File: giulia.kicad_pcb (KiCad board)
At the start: 2 copper layers, 242.2 x 113.8 mm, 138 parts, among them J1 AVR-ISP-6, J2 0548190519, M2,5 MountingHole_2.7mm_M2.5_ISO73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, SW1 RESET, SW2 BOOT, U1 ATmega32A-PU, Y1 16 MHz

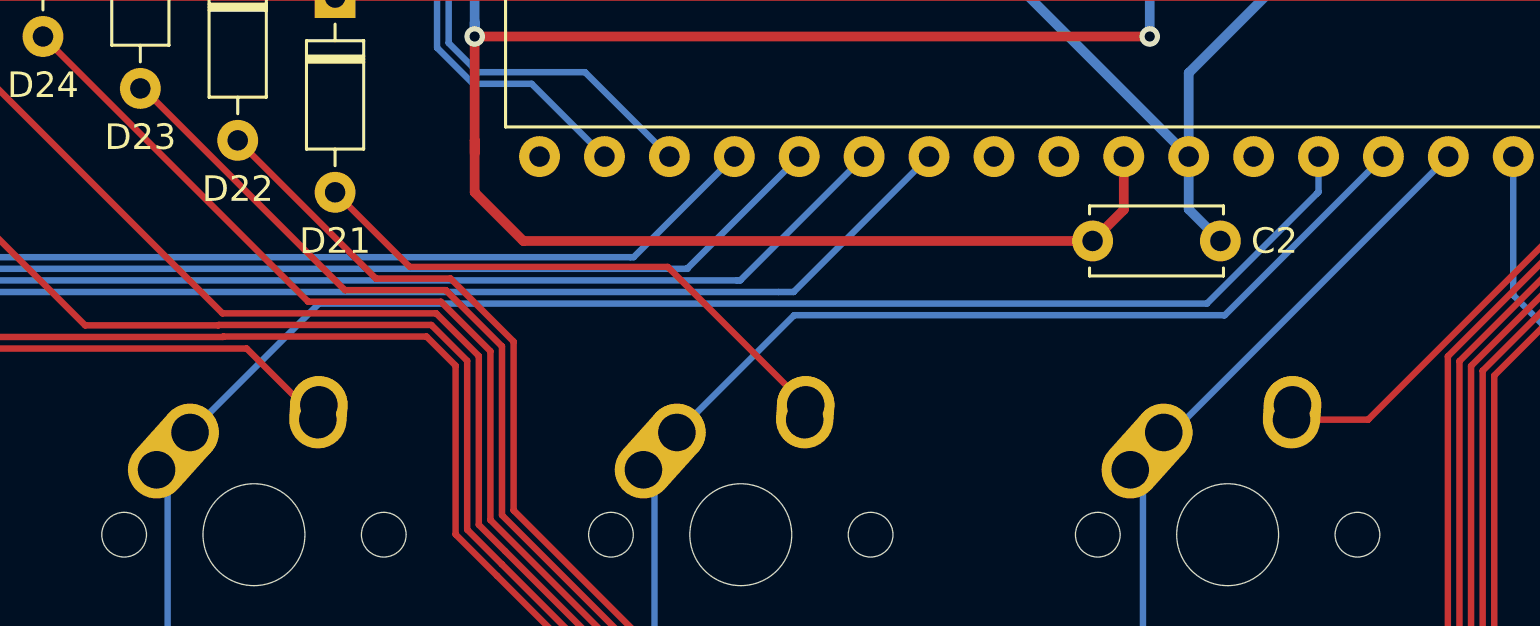
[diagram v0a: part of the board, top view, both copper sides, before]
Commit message: moved cols 4,5 to better pins
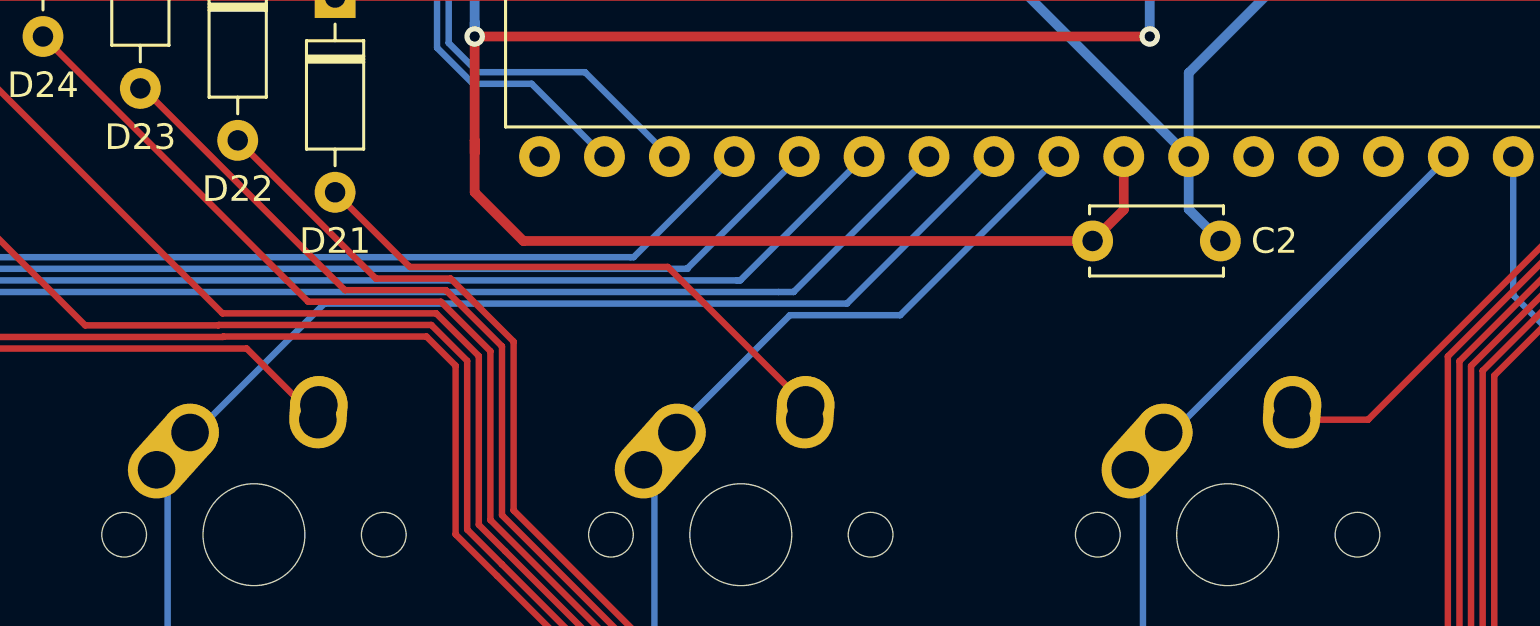
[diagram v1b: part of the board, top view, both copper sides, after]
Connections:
- U1 pad 28: Net-(U1-Pad28) -> COL4
- U1 pad 29: Net-(U1-Pad29) -> COL5
- U1 pad 33: COL4 -> Net-(U1-Pad33)
- U1 pad 34: COL5 -> Net-(U1-Pad34)
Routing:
- net COL4: track 110.1 -> 98.5 mm
- net COL5: track 92.4 -> 81.8 mm
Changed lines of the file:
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@@
     (thickness 1.6)
     (drawings 17)
-    (tracks 846)
+    (tracks 845)
     (zones 0)
     (modules 138)
@@
   (net 101 "Net-(U1-Pad14)")
   (net 102 "Net-(U1-Pad32)")
-  (net 103 "Net-(U1-Pad29)")
-  (net 104 "Net-(U1-Pad28)")
-  (net 105 "Net-(U1-Pad21)")
-  (net 106 BOOT)
-  (net 107 "Net-(U1-Pad20)")
+  (net 103 "Net-(U1-Pad21)")
+  (net 104 BOOT)
+  (net 105 "Net-(U1-Pad20)")
+  (net 106 "Net-(U1-Pad34)")
+  (net 107 "Net-(U1-Pad33)")
   (net_class Default "This is the default net class."
     (clearance 0.2)
@@
     (add_net "Net-(U1-Pad20)")
     (add_net "Net-(U1-Pad21)")
-    (add_net "Net-(U1-Pad28)")
-    (add_net "Net-(U1-Pad29)")
     (add_net "Net-(U1-Pad32)")
+    (add_net "Net-(U1-Pad33)")
+    (add_net "Net-(U1-Pad34)")
     (add_net RGB)
     (add_net ROW0)
@@
       (net 93 COL11))
     (pad 20 thru_hole oval (at 0 48.26 270) (size 1.6 1.6) (drill 0.8) (layers *.Cu *.Mask)
-      (net 107 "Net-(U1-Pad20)"))
+      (net 105 "Net-(U1-Pad20)"))
     (pad 39 thru_hole oval (at 15.24 2.54 270) (size 1.6 1.6) (drill 0.8) (layers *.Cu *.Mask)
       (net 92 COL10))
@@
       (net 100 "Net-(U1-Pad15)"))
     (pad 34 thru_hole oval (at 15.24 15.24 270) (size 1.6 1.6) (drill 0.8) (layers *.Cu *.Mask)
-      (net 87 COL5))
+      (net 106 "Net-(U1-Pad34)"))
     (pad 14 thru_hole oval (at 0 33.02 270) (size 1.6 1.6) (drill 0.8) (layers *.Cu *.Mask)
       (net 101 "Net-(U1-Pad14)"))
     (pad 33 thru_hole oval (at 15.24 17.78 270) (size 1.6 1.6) (drill 0.8) (layers *.Cu *.Mask)
-      (net 86 COL4))
+      (net 107 "Net-(U1-Pad33)"))
     (pad 13 thru_hole oval (at 0 30.48 270) (size 1.6 1.6) (drill 0.8) (layers *.Cu *.Mask)
       (net 3 "Net-(C4-Pad1)"))
@@
       (net 2 +5V))
     (pad 29 thru_hole oval (at 15.24 27.94 270) (size 1.6 1.6) (drill 0.8) (layers *.Cu *.Mask)
-      (net 103 "Net-(U1-Pad29)"))
+      (net 87 COL5))
     (pad 9 thru_hole oval (at 0 20.32 270) (size 1.6 1.6) (drill 0.8) (layers *.Cu *.Mask)
       (net 76 RST))
     (pad 28 thru_hole oval (at 15.24 30.48 270) (size 1.6 1.6) (drill 0.8) (layers *.Cu *.Mask)
-      (net 104 "Net-(U1-Pad28)"))
+      (net 86 COL4))
     (pad 8 thru_hole oval (at 0 17.78 270) (size 1.6 1.6) (drill 0.8) (layers *.Cu *.Mask)
       (net 78 SCK))
@@
       (net 83 COL1))
     (pad 5 thru_hole oval (at 0 10.16 270) (size 1.6 1.6) (drill 0.8) (layers *.Cu *.Mask)
-      (net 106 BOOT))
+      (net 104 BOOT))
     (pad 24 thru_hole oval (at 15.24 40.64 270) (size 1.6 1.6) (drill 0.8) (layers *.Cu *.Mask)
       (net 82 COL0))
@@
       (net 8 ROW1))
     (pad 21 thru_hole oval (at 15.24 48.26 270) (size 1.6 1.6) (drill 0.8) (layers *.Cu *.Mask)
-      (net 105 "Net-(U1-Pad21)"))
+      (net 103 "Net-(U1-Pad21)"))
     (pad 1 thru_hole rect (at 0 0 270) (size 1.6 1.6) (drill 0.8) (layers *.Cu *.Mask)
       (net 6 ROW0))
@@
     )
     (pad 1 thru_hole circle (at 6.5 0 270) (size 2 2) (drill 1.1) (layers *.Cu *.Mask)
-      (net 106 BOOT))
+      (net 104 BOOT))
     (pad 2 thru_hole circle (at 6.5 4.5 270) (size 2 2) (drill 1.1) (layers *.Cu *.Mask)
       (net 1 GND))
     (pad 1 thru_hole circle (at 0 0 270) (size 2 2) (drill 1.1) (layers *.Cu *.Mask)
-      (net 106 BOOT))
+      (net 104 BOOT))
     (pad 2 thru_hole circle (at 0 4.5 270) (size 2 2) (drill 1.1) (layers *.Cu *.Mask)
       (net 1 GND))
@@
   (segment (start 95.0475 74.4975) (end 95.0475 62.98) (width 0.254) (layer B.Cu) (net 85))
   (segment (start 95.0475 74.4975) (end 100.6875 80.1375) (width 0.254) (layer B.Cu) (net 85))
-  (segment (start 120.01746 56.04504) (end 114.975 61.0875) (width 0.254) (layer B.Cu) (net 86))
   (segment (start 123.19 112.40375) (end 117.35625 118.2375) (width 0.254) (layer B.Cu) (net 86))
-  (segment (start 154.76333 56.04504) (end 120.01746 56.04504) (width 0.254) (layer B.Cu) (net 86))
-  (segment (start 159.131 51.67737) (end 159.061685 51.746685) (width 0.254) (layer B.Cu) (net 86))
-  (segment (start 159.131 50.292) (end 159.131 51.67737) (width 0.254) (layer B.Cu) (net 86))
-  (segment (start 159.061685 51.746685) (end 154.76333 56.04504) (width 0.254) (layer B.Cu) (net 86))
   (segment (start 114.0975 62.98) (end 113.665 62.5475) (width 0.254) (layer B.Cu) (net 86))
   (segment (start 114.0975 74.4975) (end 114.0975 62.98) (width 0.254) (layer B.Cu) (net 86))
@@
   (segment (start 123.698 111.89575) (end 123.19 112.40375) (width 0.254) (layer B.Cu) (net 86))
   (segment (start 123.698 101.346) (end 123.698 111.89575) (width 0.254) (layer B.Cu) (net 86))
-  (segment (start 138.61345 56.49905) (end 134.025 61.0875) (width 0.254) (layer B.Cu) (net 87))
-  (segment (start 155.46395 56.49905) (end 155.43205 56.49905) (width 0.254) (layer B.Cu) (net 87))
-  (segment (start 161.671 50.292) (end 155.46395 56.49905) (width 0.254) (layer B.Cu) (net 87))
-  (segment (start 155.43205 56.49905) (end 138.61345 56.49905) (width 0.254) (layer B.Cu) (net 87))
+  (segment (start 113.7285 62.5475) (end 120.23096 56.04504) (width 0.254) (layer B.Cu) (net 86))
+  (segment (start 113.665 62.5475) (end 113.7285 62.5475) (width 0.254) (layer B.Cu) (net 86))
+  (segment (start 140.67796 56.04504) (end 146.431 50.292) (width 0.254) (layer B.Cu) (net 86))
+  (segment (start 120.23096 56.04504) (end 140.67796 56.04504) (width 0.254) (layer B.Cu) (net 86))
   (segment (start 142.736 112.661) (end 142.736 101.1435) (width 0.254) (layer B.Cu) (net 87))
   (segment (start 142.736 101.1435) (end 142.24 100.6475) (width 0.254) (layer B.Cu) (net 87))
@@
   (segment (start 133.1475 74.4975) (end 133.1475 62.98) (width 0.254) (layer B.Cu) (net 87))
   (segment (start 133.1475 74.4975) (end 138.7875 80.1375) (width 0.254) (layer B.Cu) (net 87))
+  (segment (start 132.715 62.23) (end 138.44595 56.49905) (width 0.254) (layer B.Cu) (net 87))
+  (segment (start 132.715 62.5475) (end 132.715 62.23) (width 0.254) (layer B.Cu) (net 87))
+  (segment (start 142.76395 56.49905) (end 148.971 50.292) (width 0.254) (layer B.Cu) (net 87))
+  (segment (start 138.44595 56.49905) (end 142.76395 56.49905) (width 0.254) (layer B.Cu) (net 87))
   (segment (start 153.6695 61.0875) (end 153.075 61.0875) (width 0.254) (layer B.Cu) (net 88))
   (segment (start 153.4155 61.0875) (end 153.075 61.0875) (width 0.254) (layer B.Cu) (net 88))
@@
   (segment (start 133.731 34.29) (end 133.731 35.052) (width 0.254) (layer F.Cu) (net 98))
   (segment (start 131.699 32.258) (end 133.731 34.29) (width 0.254) (layer F.Cu) (net 98))
-  (segment (start 183.307999 30.791001) (end 184.635 29.464) (width 0.254) (layer F.Cu) (net 106))
-  (segment (start 184.635 29.464) (end 191.135 29.464) (width 0.254) (layer F.Cu) (net 106))
-  (segment (start 171.011999 30.791001) (end 183.307999 30.791001) (width 0.254) (layer F.Cu) (net 106))
-  (segment (start 166.751 35.052) (end 171.011999 30.791001) (width 0.254) (layer F.Cu) (net 106))
-  (segment (start 128.905 35.052) (end 128.651 35.052) (width 0.254) (layer F.Cu) (net 107))
+  (segment (start 183.307999 30.791001) (end 184.635 29.464) (width 0.254) (layer F.Cu) (net 104))
+  (segment (start 184.635 29.464) (end 191.135 29.464) (width 0.254) (layer F.Cu) (net 104))
+  (segment (start 171.011999 30.791001) (end 183.307999 30.791001) (width 0.254) (layer F.Cu) (net 104))
+  (segment (start 166.751 35.052) (end 171.011999 30.791001) (width 0.254) (layer F.Cu) (net 104))
+  (segment (start 128.905 35.052) (end 128.651 35.052) (width 0.254) (layer F.Cu) (net 105))
 )

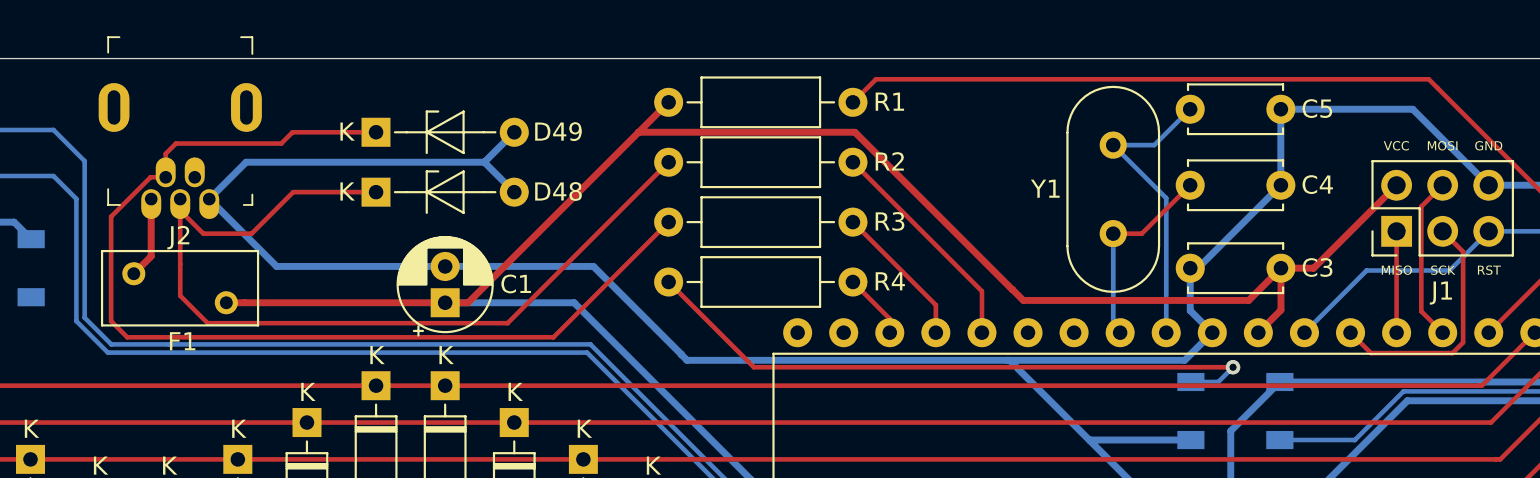
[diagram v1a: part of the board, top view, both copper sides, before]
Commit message: moved resistors for visual alignment
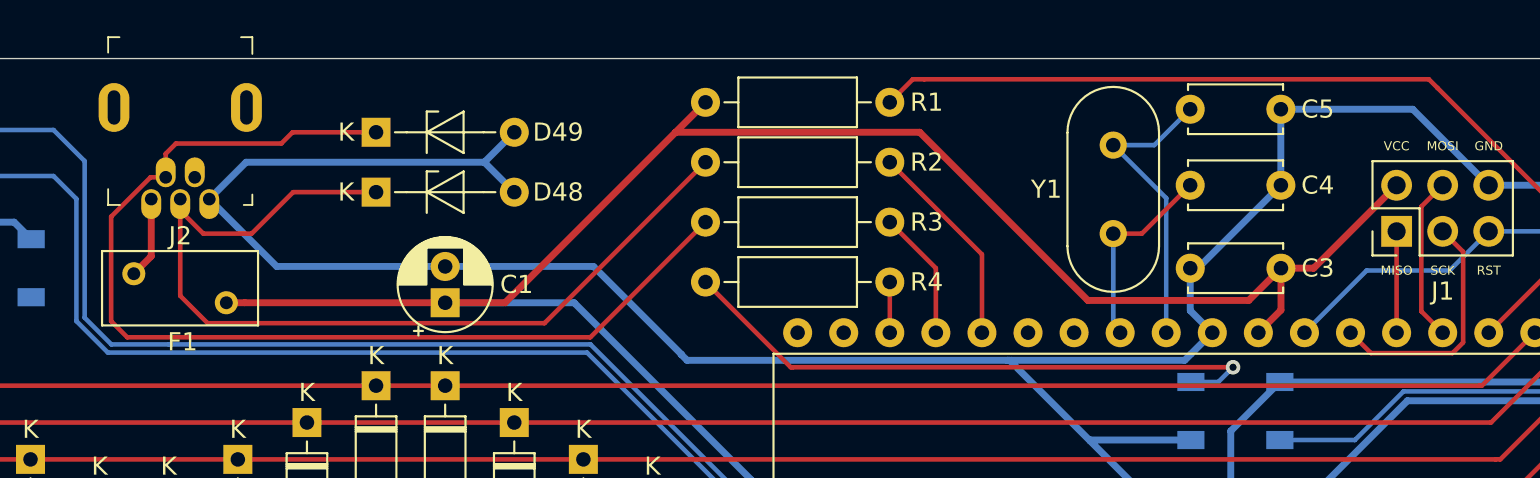
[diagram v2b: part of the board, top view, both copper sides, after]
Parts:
- moved R1 2.03 mm to (123.6, 22.4)
- moved R4 2.03 mm to (123.6, 32.3)
- moved R2 2.03 mm to (133.7, 25.7)
- moved R3 2.03 mm to (133.7, 29.0)
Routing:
- net Net-(D49-Pad1): track 57.0 -> 59.0 mm
- net Net-(D50-Pad4): track 35.7 -> 33.7 mm
- net Net-(D48-Pad1): track 49.7 -> 51.7 mm
- net RST: track 68.2 -> 66.2 mm
- net RGB: track 3.64 -> 2.79 mm
- net D-: track 7.99 -> 7.15 mm
- net D+: track 12.3 -> 11.5 mm

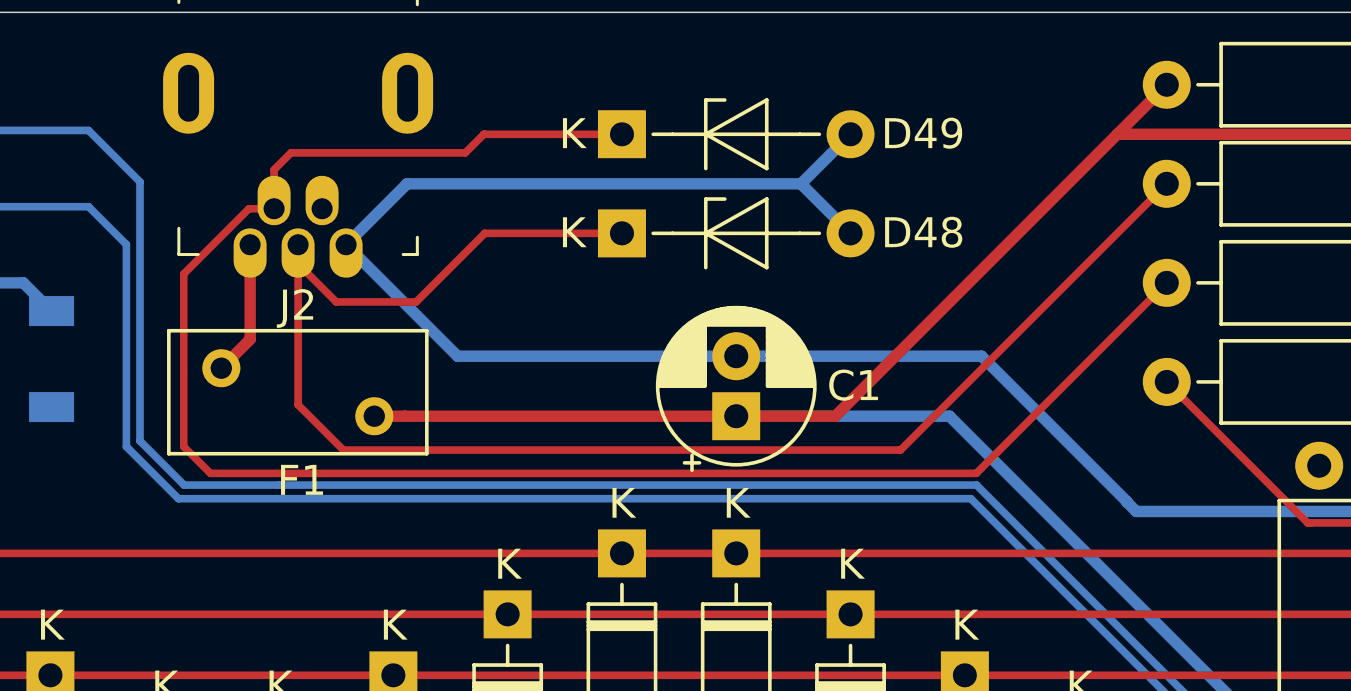
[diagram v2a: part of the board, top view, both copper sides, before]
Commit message: moved USB data lines
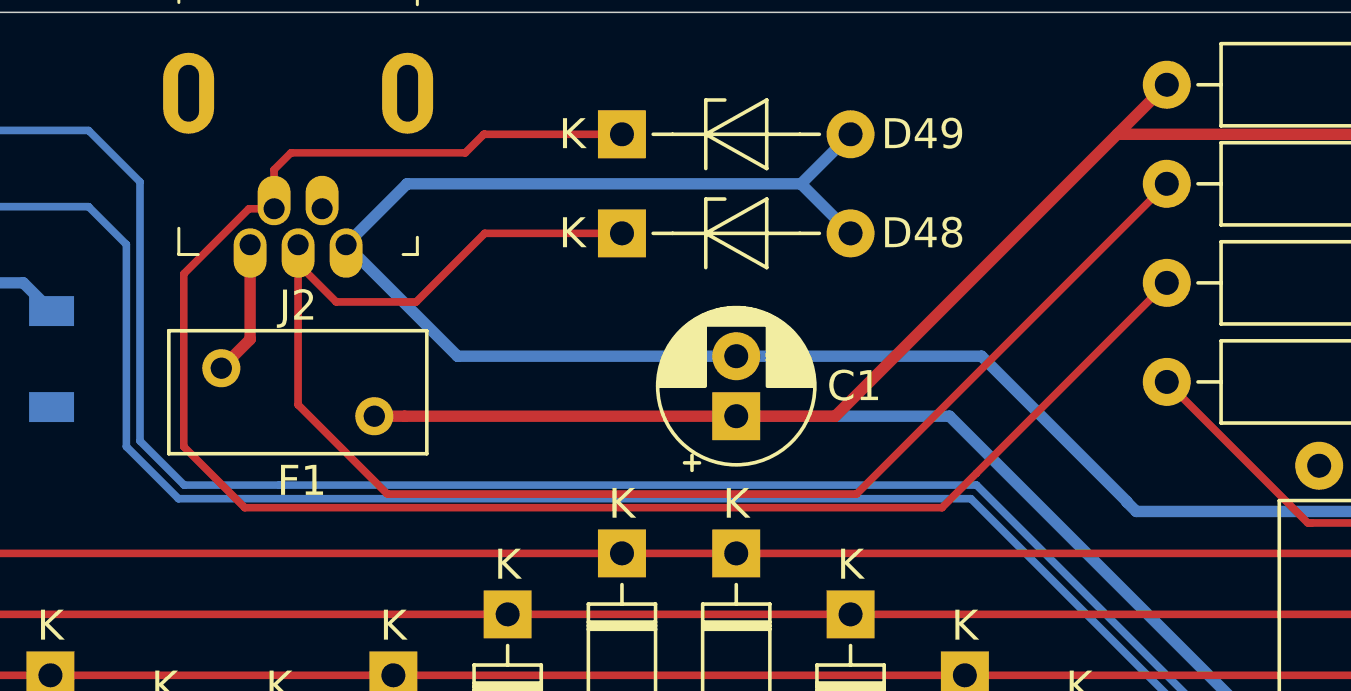
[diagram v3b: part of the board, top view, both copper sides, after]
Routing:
- net Net-(D48-Pad1): track 51.7 -> 52.9 mm
- net Net-(D49-Pad1): track 59.0 -> 60.0 mm
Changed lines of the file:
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@@
     (thickness 1.6)
     (drawings 17)
-    (tracks 842)
+    (tracks 843)
     (zones 0)
     (modules 138)
@@
   (segment (start 94.615 28.321) (end 95.885 29.591) (width 0.254) (layer F.Cu) (net 56))
   (segment (start 94.615 27.686) (end 94.615 28.321) (width 0.254) (layer F.Cu) (net 56))
-  (segment (start 114.696999 34.528001) (end 123.571 25.654) (width 0.254) (layer F.Cu) (net 56))
-  (segment (start 96.123001 34.528001) (end 114.696999 34.528001) (width 0.254) (layer F.Cu) (net 56))
-  (segment (start 94.615 33.02) (end 96.123001 34.528001) (width 0.254) (layer F.Cu) (net 56))
   (segment (start 94.615 27.686) (end 94.615 33.02) (width 0.254) (layer F.Cu) (net 56))
+  (segment (start 123.571 25.654) (end 113.23001 35.99499) (width 0.254) (layer F.Cu) (net 56))
+  (segment (start 97.58999 35.99499) (end 94.615 33.02) (width 0.254) (layer F.Cu) (net 56))
+  (segment (start 113.23001 35.99499) (end 97.58999 35.99499) (width 0.254) (layer F.Cu) (net 56))
   (segment (start 93.815 26.486) (end 93.815 26.295721) (width 0.254) (layer F.Cu) (net 57))
   (segment (start 100.838 24.003) (end 105.41 24.003) (width 0.254) (layer F.Cu) (net 57))
@@
   (segment (start 93.815 26.486) (end 93.815 25.184) (width 0.254) (layer F.Cu) (net 57))
   (segment (start 117.221 35.306) (end 123.571 28.956) (width 0.254) (layer F.Cu) (net 57))
-  (segment (start 91.694 35.306) (end 117.221 35.306) (width 0.254) (layer F.Cu) (net 57))
-  (segment (start 90.805 34.417) (end 91.694 35.306) (width 0.254) (layer F.Cu) (net 57))
+  (segment (start 116.078 36.449) (end 117.221 35.306) (width 0.254) (layer F.Cu) (net 57))
+  (segment (start 92.837 36.449) (end 116.078 36.449) (width 0.254) (layer F.Cu) (net 57))
   (segment (start 90.805 28.655721) (end 90.805 34.417) (width 0.254) (layer F.Cu) (net 57))
   (segment (start 92.974721 26.486) (end 90.805 28.655721) (width 0.254) (layer F.Cu) (net 57))
+  (segment (start 90.805 34.417) (end 92.837 36.449) (width 0.254) (layer F.Cu) (net 57))
   (segment (start 93.815 26.486) (end 92.974721 26.486) (width 0.254) (layer F.Cu) (net 57))
   (segment (start 187.802622 38.28751) (end 196.194132 29.896) (width 0.254) (layer B.Cu) (net 58))
